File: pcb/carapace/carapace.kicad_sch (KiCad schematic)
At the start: 17 parts, among them J2 Würth 61201621721, P1 Qwiic verso X20, P2 catena LED, P3 microfoni, P4 amplificatore, P5 ToF posteriore, P6 pulsante, P7 riserva polo 14, U6 TCA9534 (0x20)

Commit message: D-079: arresto R1 dei PCB approvato; correzioni della verifica con due agenti (TCA9534 tolto, R16 su OFF, regole del DRC per 5V/3V3 del carapace, EN di U2 e pulsante, testata con fori da 1,1, CS su due passi, tetto dei LED a 450 mA con l'audio)
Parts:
- removed U6: TCA9534 (0x20), hex2:SOIC-16_3.9x9.9mm_P1.27mm, symbol hex2_kicad:TCA9534
- J2: footprint hex2:IDC-Header_2x08_P2.54mm_Horizontal -> hex2:IDC-Header_2x08_P2.54mm_Horizontal_Foro1.1
- P5: footprint hex2:PinHeader_1x05_P2.54mm_Vertical -> hex2:PinHeader_1x04_P2.54mm_Vertical; symbol hex2_kicad:Conn_01x05 -> hex2_kicad:Conn_01x04
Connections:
- removed net XSHUT_POST: P5.5 (Pin_5)
- no-connect marks 8 -> 0

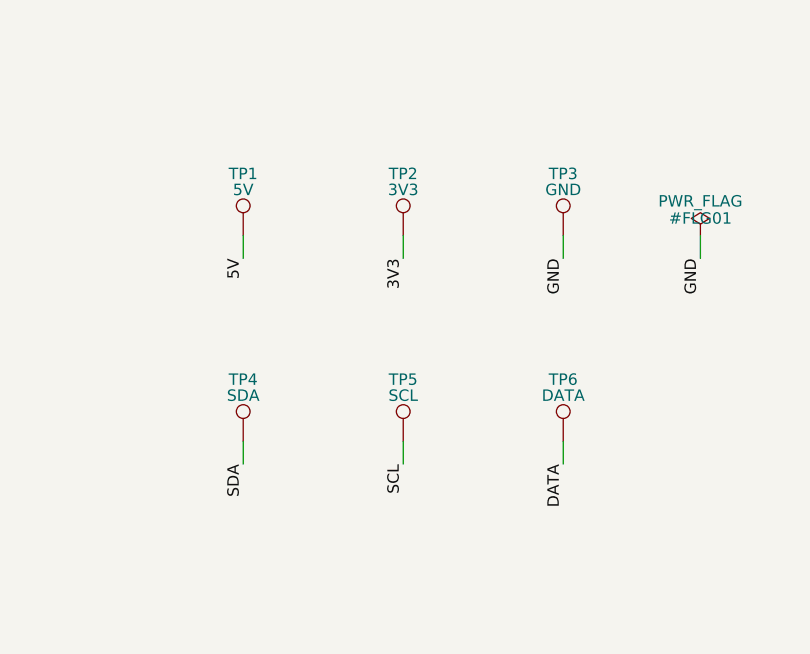
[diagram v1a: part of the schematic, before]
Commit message: PCB-C, F4: piazzamento (J2 sul bordo di coda, griglia di piazzole Ø1,5, ToF e R-MIC nell'ala +Y, CE1 in piedi nell'ala -Y con 14 mm liberi sotto); piazzole per fili proprie, zone senza rame sopra le bugne senza margine, fase di piazzamento in controlla.py; casi di controllo delle regole del pulsante e del 5V
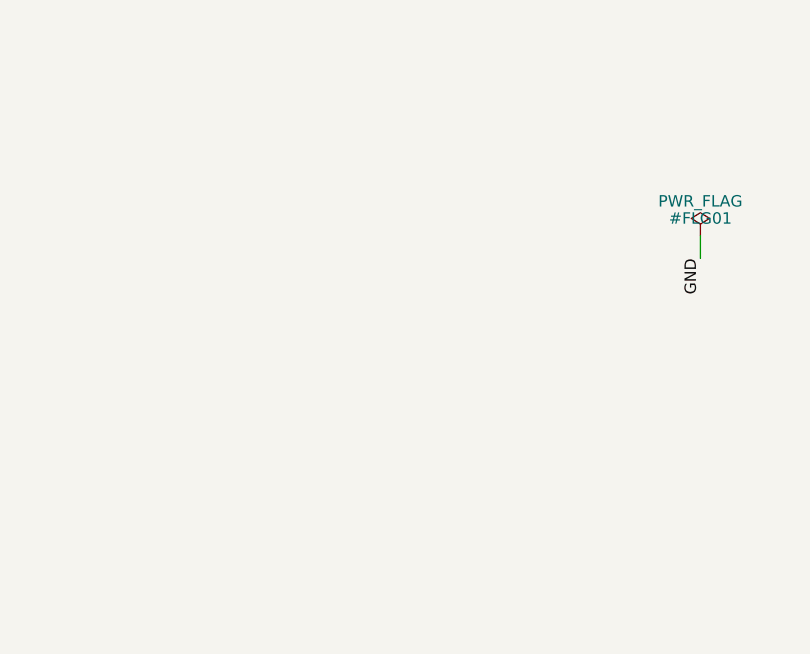
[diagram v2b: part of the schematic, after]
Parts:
- removed TP1: 5V, hex2:TestPoint_THTPad_1.5x1.5mm_Drill0.7mm, symbol hex2_kicad:TestPoint
- removed TP2: 3V3, hex2:TestPoint_THTPad_1.5x1.5mm_Drill0.7mm, symbol hex2_kicad:TestPoint
- removed TP3: GND, hex2:TestPoint_THTPad_1.5x1.5mm_Drill0.7mm, symbol hex2_kicad:TestPoint
- removed TP4: SDA, hex2:TestPoint_THTPad_1.5x1.5mm_Drill0.7mm, symbol hex2_kicad:TestPoint
- removed TP5: SCL, hex2:TestPoint_THTPad_1.5x1.5mm_Drill0.7mm, symbol hex2_kicad:TestPoint
- removed TP6: DATA, hex2:TestPoint_THTPad_1.5x1.5mm_Drill0.7mm, symbol hex2_kicad:TestPoint
- CE1: footprint hex2:CP_Radial_D6.3mm_P2.50mm_Sdraiato -> hex2:CP_Radial_D6.3mm_P2.50mm
- P1: footprint hex2:PinHeader_1x04_P2.54mm_Vertical -> hex2:Fili_1x04_P2.54mm_D1.5
- P2: footprint hex2:PinHeader_1x03_P2.54mm_Vertical -> hex2:Fili_1x03_P2.54mm_D1.5
- P3, P4: footprint hex2:PinHeader_1x05_P2.54mm_Vertical -> hex2:Fili_1x05_P2.54mm_D1.5
- P5: footprint hex2:PinHeader_1x04_P2.54mm_Vertical -> hex2:Fili_2x02_P2.54mm_D1.5
- P6: footprint hex2:PinHeader_1x02_P2.54mm_Vertical -> hex2:Fili_1x02_P2.54mm_D1.5
- P7: footprint hex2:PinHeader_1x01_P2.54mm_Vertical -> hex2:Fili_1x01_P2.54mm_D1.5
- R1: footprint hex2:R_Axial_DIN0207_L6.3mm_D2.5mm_P7.62mm_Horizontal -> hex2:R_Axial_DIN0207_L6.3mm_D2.5mm_P2.54mm_Vertical

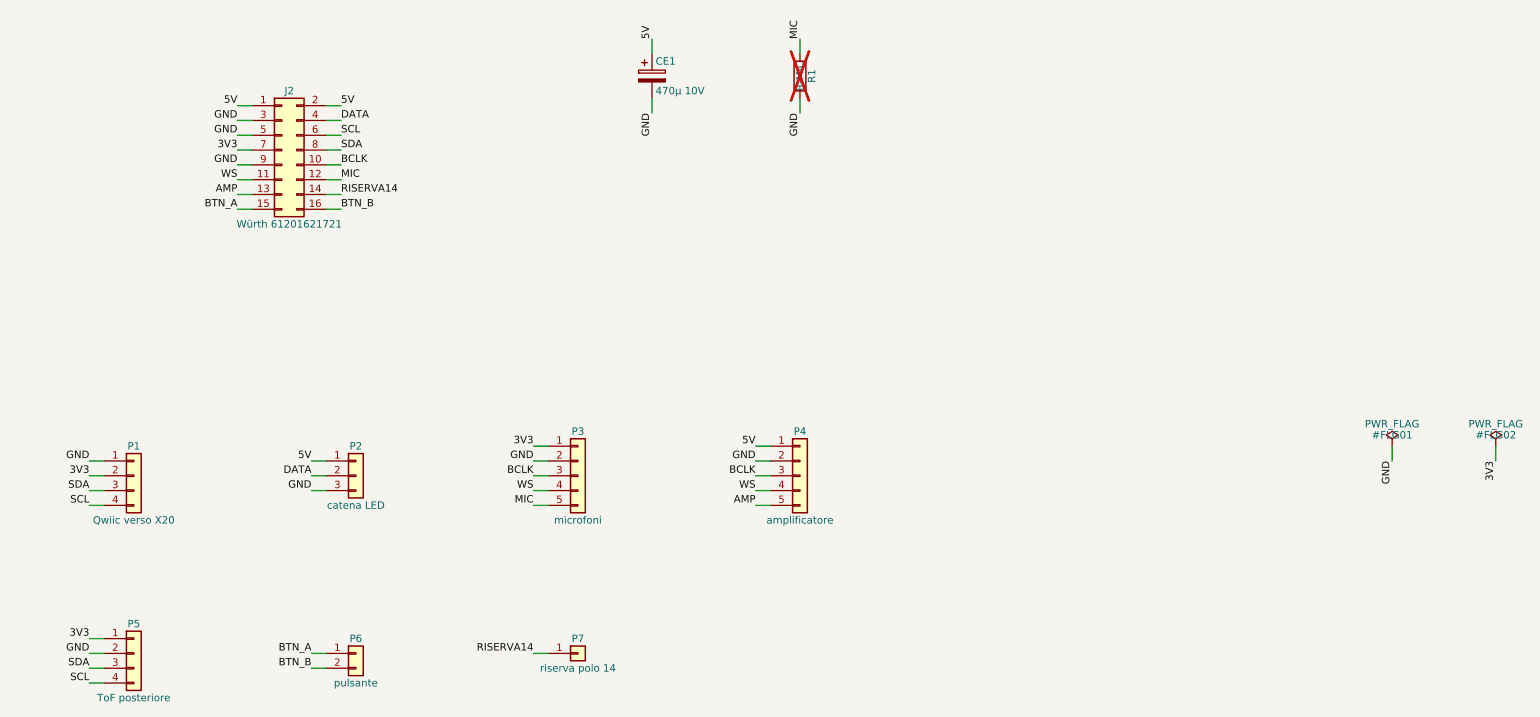
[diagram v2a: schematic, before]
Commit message: D-082: correzioni della revisione indipendente (17 agenti): PCB-C rifatta e sbrogliata da script (DRC a zero), regole del DRC corrette (una scritta male faceva ignorare il file), piazzole dei fili in verifica_reti, ali da 5,5, JP-RMT 680/1k, tetto dei LED 600/400 mA, guida 8.10/8.22/8.24, CI con KiCad obbligatorio; proposta della 2.1.9 (scheda dei partitori piu' grande)
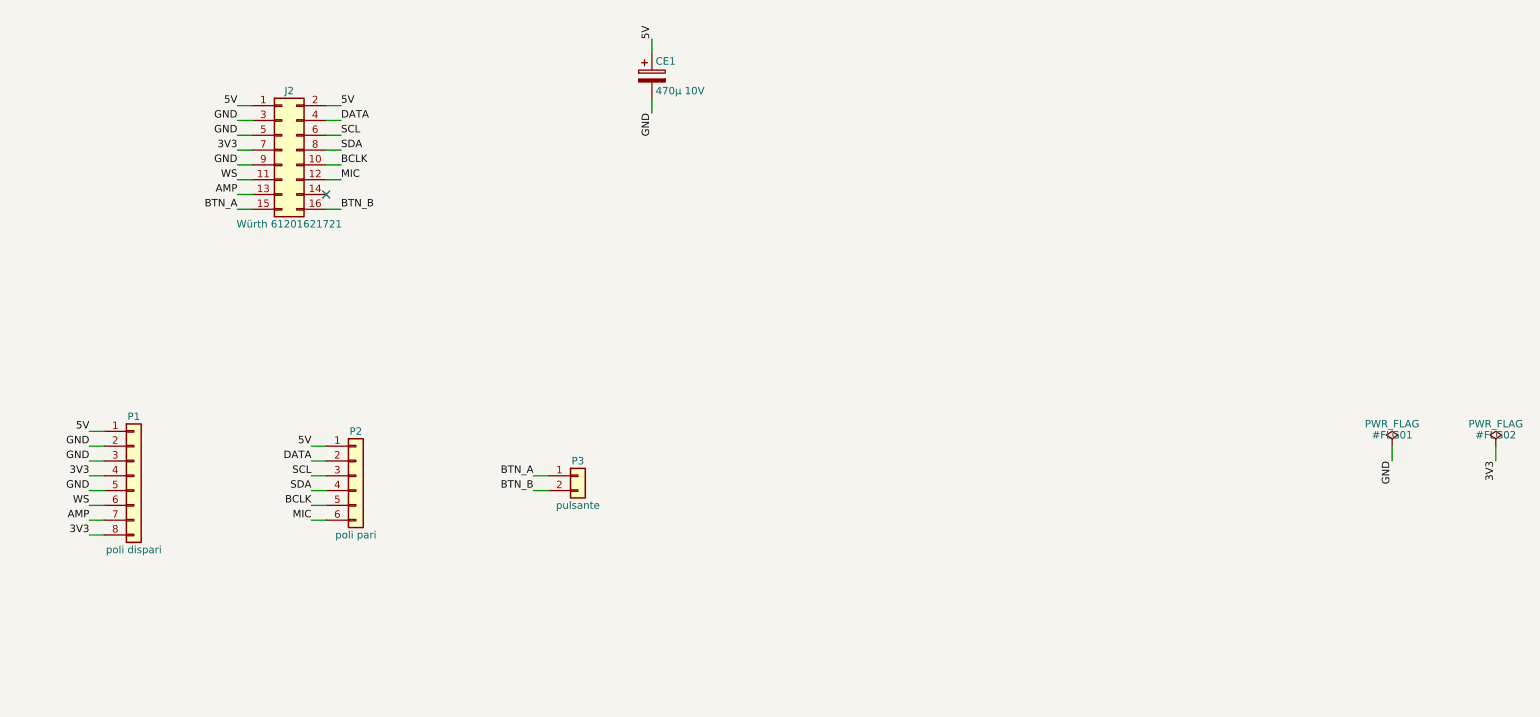
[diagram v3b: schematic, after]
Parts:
- removed P4: amplificatore, hex2:Fili_1x05_P2.54mm_D1.5, symbol hex2_kicad:Conn_01x05
- removed P5: ToF posteriore, hex2:Fili_2x02_P2.54mm_D1.5, symbol hex2_kicad:Conn_01x04
- removed P6: pulsante, hex2:Fili_1x02_P2.54mm_D1.5, symbol hex2_kicad:Conn_01x02
- removed P7: riserva polo 14, hex2:Fili_1x01_P2.54mm_D1.5, symbol hex2_kicad:Conn_01x01
- removed R1: R-MIC, hex2:R_Axial_DIN0207_L6.3mm_D2.5mm_P2.54mm_Vertical, symbol hex2_kicad:R
- P1: value Qwiic verso X20 -> poli dispari; footprint hex2:Fili_1x04_P2.54mm_D1.5 -> hex2:Fili_1x08_P2.54mm_D1.7; symbol hex2_kicad:Conn_01x04 -> hex2_kicad:Conn_01x08
- P2: value catena LED -> poli pari; footprint hex2:Fili_1x03_P2.54mm_D1.5 -> hex2:Fili_1x06_P2.54mm_D1.7; symbol hex2_kicad:Conn_01x03 -> hex2_kicad:Conn_01x06
- P3: value microfoni -> pulsante; footprint hex2:Fili_1x05_P2.54mm_D1.5 -> hex2:Fili_1x02_P2.54mm_D1.7; symbol hex2_kicad:Conn_01x05 -> hex2_kicad:Conn_01x02
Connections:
- net 3V3: now also P1.4 (Pin_4), P1.8 (Pin_8); no longer P1.2 (Pin_2), P3.1 (Pin_1)
- net 5V: now also P1.1 (Pin_1)
- net AMP: now also P1.7 (Pin_7)
- net BCLK: now also P2.5 (Pin_5); no longer P3.3 (Pin_3)
- net BTN_A: now also P3.1 (Pin_1)
- net BTN_B: now also P3.2 (Pin_2)
- net GND: now also P1.2 (Pin_2), P1.3 (Pin_3), P1.5 (Pin_5); no longer P1.1 (Pin_1), P2.3 (Pin_3), P3.2 (Pin_2)
- net MIC: now also P2.6 (Pin_6); no longer P3.5 (Pin_5)
- net SCL: now also P2.3 (Pin_3); no longer P1.4 (Pin_4)
- net SDA: now also P2.4 (Pin_4); no longer P1.3 (Pin_3)
- net WS: now also P1.6 (Pin_6); no longer P3.4 (Pin_4)
- net RISERVA14: no longer names the net of J2.14 (Pin_14)
- no-connect marks 0 -> 1
